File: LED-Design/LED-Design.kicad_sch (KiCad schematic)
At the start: 160 parts, among them Q1 NMOS, Q2 NMOS, Q3 NMOS, Q4 NMOS, Q5 NMOS, Q6 NMOS, Q7 NMOS, U1 74LS573, U2 74LS573, U3 74LS573, U4 74LS573, U6 74HC164

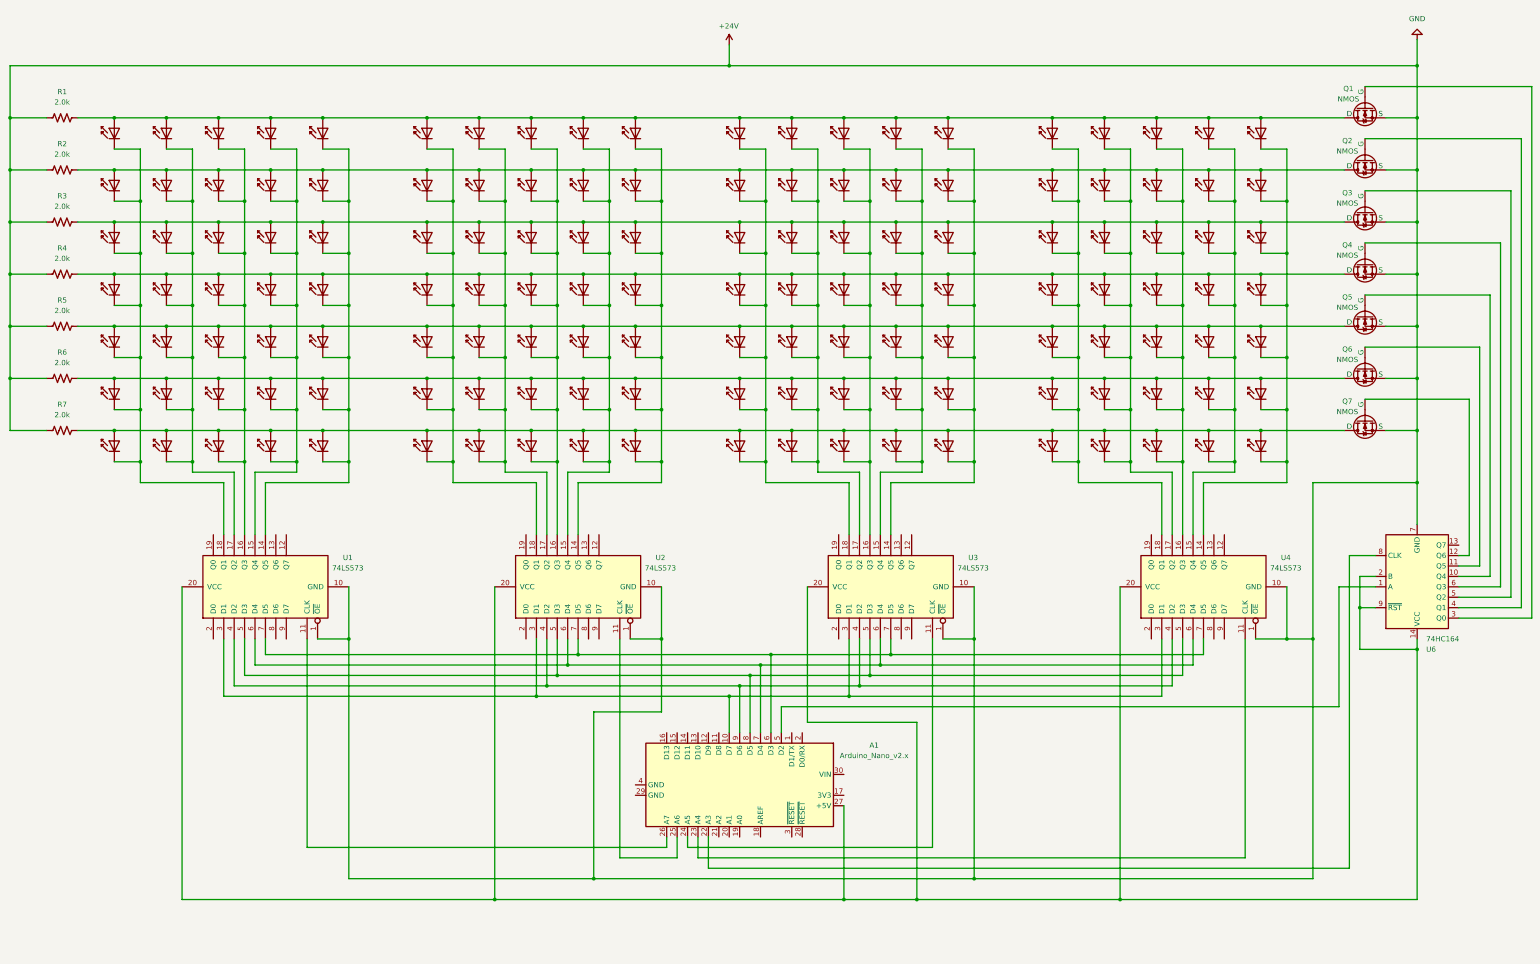
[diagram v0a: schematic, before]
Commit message: Added a Voltage divider
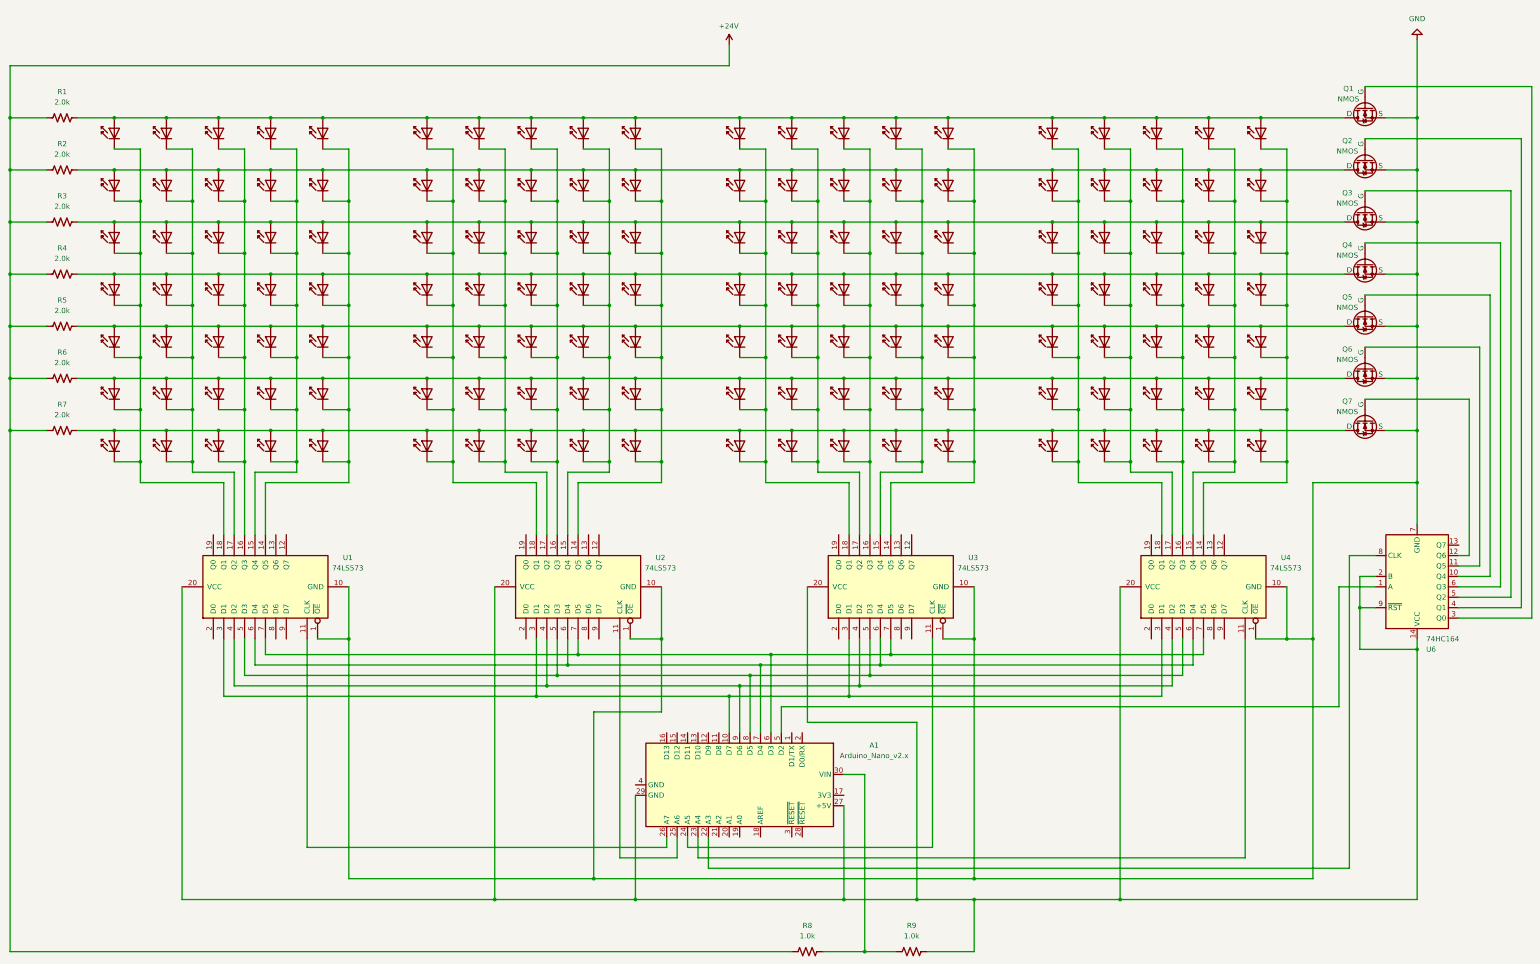
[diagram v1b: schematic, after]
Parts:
- added R8, R9: 1.0k, OptoDevice:R_LDR_5.2x5.2mm_P3.5mm_Horizontal, symbol Device:R_US
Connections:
- net +24V: now also R8.1; no longer Q1.3 (S), Q2.3 (S), Q3.3 (S), Q4.3 (S), Q5.3 (S), Q6.3 (S), Q7.3 (S), U1.1 (~{OE}), U1.10 (GND), U2.1 (~{OE}), U2.10 (GND), U3.1 (~{OE}), U3.10 (GND), U4.1 (~{OE}), U4.10 (GND), U6.7 (GND)
- net at A1.27 (+5V), U1.20 (VCC), U2.20 (VCC)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: now also A1.29 (GND), R9.2
- net at A1.30 (VIN): now also R8.2, R9.1
- new net GND: Q1.3 (S), Q2.3 (S), Q3.3 (S), Q4.3 (S), Q5.3 (S), Q6.3 (S), Q7.3 (S), U1.1 (~{OE}), U1.10 (GND), U2.1 (~{OE}), U2.10 (GND), U3.1 (~{OE}), U3.10 (GND), U4.1 (~{OE}), U4.10 (GND), U6.7 (GND)
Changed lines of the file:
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@@
 	)
 	(junction
+		(at 25.4 127)
+		(diameter 0)
+		(color 0 0 0 0)
+	)
+	(junction
 		(at 208.28 184.15)
 		(diameter 0)
@@
 	)
 	(junction
-		(at 200.66 38.1)
-		(diameter 0)
-		(color 0 0 0 0)
-	)
-	(junction
 		(at 127 88.9)
 		(diameter 0)
@@
 	)
 	(junction
+		(at 260.35 241.3)
+		(diameter 0)
+		(color 0 0 0 0)
+	)
+	(junction
 		(at 88.9 76.2)
 		(diameter 0)
@@
 	)
 	(junction
-		(at 368.3 38.1)
-		(diameter 0)
-		(color 0 0 0 0)
-	)
-	(junction
 		(at 285.75 134.62)
 		(diameter 0)
@@
 	)
 	(junction
+		(at 177.8 241.3)
+		(diameter 0)
+		(color 0 0 0 0)
+	)
+	(junction
 		(at 292.1 50.8)
 		(diameter 0)
@@
 	)
 	(junction
+		(at 233.68 254)
+		(diameter 0)
+		(color 0 0 0 0)
+	)
+	(junction
 		(at 76.2 50.8)
 		(diameter 0)
@@
 	(wire
 		(pts
+			(xy 215.9 254) (xy 25.4 254)
+		)
+		(stroke
+			(width 0)
+			(type default)
+		)
+	)
+	(wire
+		(pts
 			(xy 317.5 127) (xy 330.2 127)
 		)
@@
 	(wire
 		(pts
+			(xy 228.6 210.82) (xy 233.68 210.82)
+		)
+		(stroke
+			(width 0)
+			(type default)
+		)
+	)
+	(wire
+		(pts
 			(xy 279.4 63.5) (xy 292.1 63.5)
 		)
@@
 	(wire
 		(pts
-			(xy 246.38 241.3) (xy 295.91 241.3)
+			(xy 246.38 241.3) (xy 260.35 241.3)
 		)
 		(stroke
@@
 	(wire
 		(pts
-			(xy 368.3 31.75) (xy 368.3 38.1)
+			(xy 368.3 31.75) (xy 368.3 50.8)
 		)
 		(stroke
@@
 	(wire
 		(pts
+			(xy 177.8 215.9) (xy 177.8 241.3)
+		)
+		(stroke
+			(width 0)
+			(type default)
+		)
+	)
+	(wire
+		(pts
 			(xy 396.24 43.18) (xy 396.24 172.72)
 		)
@@
 	(wire
 		(pts
-			(xy 143.51 241.3) (xy 228.6 241.3)
+			(xy 143.51 241.3) (xy 177.8 241.3)
 		)
 		(stroke
@@
 	(wire
 		(pts
+			(xy 25.4 254) (xy 25.4 127)
+		)
+		(stroke
+			(width 0)
+			(type default)
+		)
+	)
+	(wire
+		(pts
 			(xy 76.2 50.8) (xy 88.9 50.8)
 		)
@@
 	(wire
 		(pts
+			(xy 260.35 254) (xy 260.35 241.3)
+		)
+		(stroke
+			(width 0)
+			(type default)
+		)
+	)
+	(wire
+		(pts
 			(xy 133.35 134.62) (xy 133.35 139.7)
 		)
@@
 	(wire
 		(pts
+			(xy 233.68 254) (xy 241.3 254)
+		)
+		(stroke
+			(width 0)
+			(type default)
+		)
+	)
+	(wire
+		(pts
 			(xy 63.5 63.5) (xy 76.2 63.5)
 		)
@@
 	(wire
 		(pts
+			(xy 248.92 254) (xy 260.35 254)
+		)
+		(stroke
+			(width 0)
+			(type default)
+		)
+	)
+	(wire
+		(pts
 			(xy 50.8 114.3) (xy 63.5 114.3)
 		)
@@
 	(wire
 		(pts
+			(xy 223.52 254) (xy 233.68 254)
+		)
+		(stroke
+			(width 0)
+			(type default)
+		)
+	)
+	(wire
+		(pts
 			(xy 101.6 96.52) (xy 107.95 96.52)
 		)
@@
 	(wire
 		(pts
+			(xy 260.35 241.3) (xy 295.91 241.3)
+		)
+		(stroke
+			(width 0)
+			(type default)
+		)
+	)
+	(wire
+		(pts
+			(xy 233.68 210.82) (xy 233.68 254)
+		)
+		(stroke
+			(width 0)
+			(type default)
+		)
+	)
+	(wire
+		(pts
 			(xy 76.2 121.92) (xy 82.55 121.92)
 		)
@@
 	(wire
 		(pts
-			(xy 200.66 38.1) (xy 368.3 38.1)
-		)
-		(stroke
-			(width 0)
-			(type default)
-		)
-	)
-	(wire
-		(pts
 			(xy 240.03 152.4) (xy 240.03 139.7)
 		)
@@
 	(wire
 		(pts
-			(xy 368.3 50.8) (xy 368.3 38.1)
-		)
-		(stroke
-			(width 0)
-			(type default)
-		)
-	)
-	(wire
-		(pts
 			(xy 139.7 127) (xy 152.4 127)
 		)
@@
 	(wire
 		(pts
+			(xy 177.8 241.3) (xy 228.6 241.3)
+		)
+		(stroke
+			(width 0)
+			(type default)
+		)
+	)
+	(wire
+		(pts
 			(xy 41.91 127) (xy 50.8 127)
 		)
@@
 	)
 	(symbol
+		(lib_id "Device:R_US")
+		(at 245.11 254 90)
+		(unit 1)
+		(exclude_from_sim no)
+		(in_bom yes)
+		(on_board yes)
+		(dnp no)
+		(fields_autoplaced yes)
+		(property "Reference" "R9"
+			(at 245.11 247.65 90)
+			(effects
+				(font
+					(size 1.27 1.27)
+				)
+			)
+		)
+		(property "Value" "1.0k"
+			(at 245.11 250.19 90)
+			(effects
+				(font
+					(size 1.27 1.27)
+				)
+			)
+		)
+		(property "Footprint" "OptoDevice:R_LDR_5.2x5.2mm_P3.5mm_Horizontal"
+			(at 245.364 252.984 90)
+			(effects
+				(font
+					(size 1.27 1.27)
+				)
+				(hide yes)
+			)
+		)
+		(property "Datasheet" "~"
+			(at 245.11 254 0)
+			(effects
+				(font
+					(size 1.27 1.27)
+				)
+				(hide yes)
+			)
+		)
+		(property "Description" "Resistor, US symbol"
+			(at 245.11 254 0)
+			(effects
+				(font
+					(size 1.27 1.27)
+				)
+				(hide yes)
+			)
+		)
+		(pin "1"
+		)
+		(pin "2"
+		)
+		(instances
+			(project "LED-Design"
+				(path "/f4f73743-e943-40e7-b3a9-52df178c6ab8"
+					(reference "R9")
+					(unit 1)
+				)
+			)
+		)
+	)
+	(symbol
 		(lib_id "LED:IR204A")
 		(at 76.2 78.74 90)
@@
 					(unit 1)
 				)
+			)
+		)
+	)
+	(symbol
+		(lib_id "Device:R_US")
+		(at 219.71 254 90)
+		(unit 1)
+		(exclude_from_sim no)
+		(in_bom yes)
+		(on_board yes)
+		(dnp no)
+		(fields_autoplaced yes)
+		(property "Reference" "R8"
+			(at 219.71 247.65 90)
+			(effects
+				(font
+					(size 1.27 1.27)
+				)
+			)
+		)
+		(property "Value" "1.0k"
+			(at 219.71 250.19 90)
+			(effects
+				(font
+					(size 1.27 1.27)
+				)
+			)
+		)
+		(property "Footprint" "OptoDevice:R_LDR_5.2x5.2mm_P3.5mm_Horizontal"
+			(at 219.964 252.984 90)
+			(effects
+				(font
+					(size 1.27 1.27)
+				)
+				(hide yes)
+			)
+		)
+		(property "Datasheet" "~"
+			(at 219.71 254 0)
+			(effects
+				(font
+					(size 1.27 1.27)
+				)
+				(hide yes)
+			)
+		)
+		(property "Description" "Resistor, US symbol"
+			(at 219.71 254 0)
+			(effects
+				(font
+					(size 1.27 1.27)
+				)
+				(hide yes)
+			)
+		)
+		(pin "1"
+		)
+		(pin "2"
+		)
+		(instances
+			(project "LED-Design"
+				(path "/f4f73743-e943-40e7-b3a9-52df178c6ab8"
+					(reference "R8")
+					(unit 1)
+				)

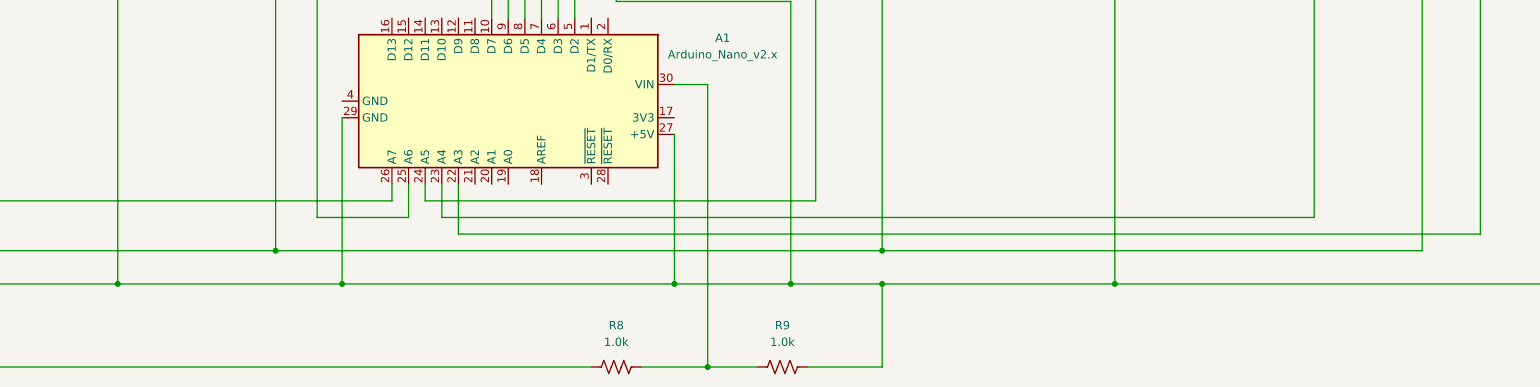
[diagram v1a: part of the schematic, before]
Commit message: Added all components to the schematic and linked them to their footprints
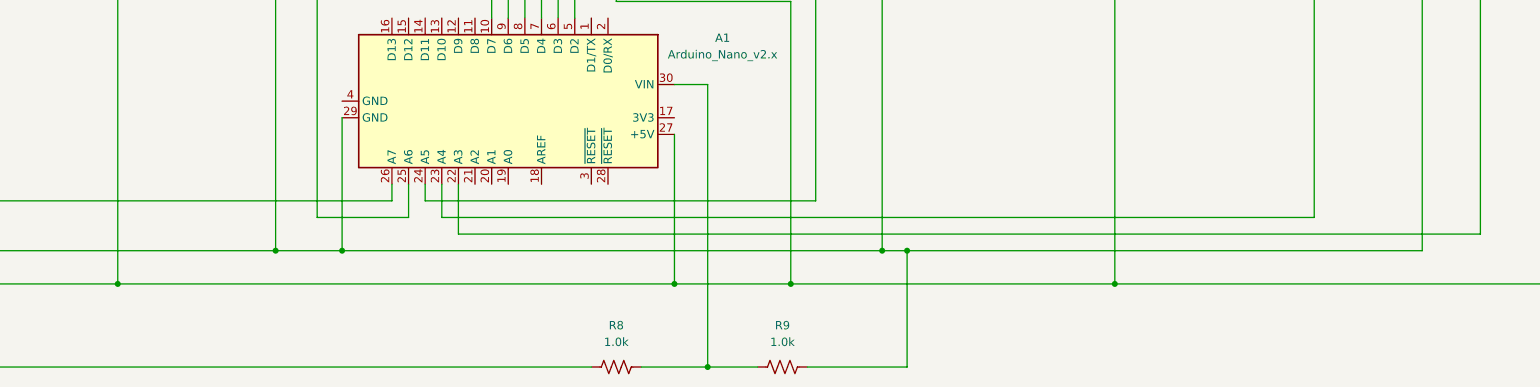
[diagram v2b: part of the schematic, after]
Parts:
- Q1, Q2, Q3, Q4, Q5, Q6, Q7: footprint (none) -> Package_TO_SOT_THT:TO-220-3_Vertical
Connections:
- net GND: now also A1.29 (GND), R9.2
- net at A1.27 (+5V), U1.20 (VCC), U2.20 (VCC)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: no longer A1.29 (GND), R9.2
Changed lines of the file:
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@@
 	)
 	(junction
+		(at 264.16 236.22)
+		(diameter 0)
+		(color 0 0 0 0)
+	)
+	(junction
 		(at 215.9 63.5)
 		(diameter 0)
@@
 	)
 	(junction
+		(at 177.8 236.22)
+		(diameter 0)
+		(color 0 0 0 0)
+	)
+	(junction
 		(at 246.38 241.3)
 		(diameter 0)
@@
 	)
 	(junction
-		(at 260.35 241.3)
-		(diameter 0)
-		(color 0 0 0 0)
-	)
-	(junction
 		(at 88.9 76.2)
 		(diameter 0)
@@
 	)
 	(junction
-		(at 177.8 241.3)
-		(diameter 0)
-		(color 0 0 0 0)
-	)
-	(junction
 		(at 292.1 50.8)
 		(diameter 0)
@@
 	(wire
 		(pts
-			(xy 246.38 241.3) (xy 260.35 241.3)
-		)
-		(stroke
-			(width 0)
-			(type default)
-		)
-	)
-	(wire
-		(pts
 			(xy 69.85 58.42) (xy 69.85 71.12)
 		)
@@
 	(wire
 		(pts
+			(xy 177.8 215.9) (xy 177.8 236.22)
+		)
+		(stroke
+			(width 0)
+			(type default)
+		)
+	)
+	(wire
+		(pts
 			(xy 260.35 83.82) (xy 260.35 96.52)
 		)
@@
 	(wire
 		(pts
-			(xy 177.8 215.9) (xy 177.8 241.3)
-		)
-		(stroke
-			(width 0)
-			(type default)
-		)
-	)
-	(wire
-		(pts
 			(xy 396.24 43.18) (xy 396.24 172.72)
 		)
@@
 	(wire
 		(pts
-			(xy 143.51 241.3) (xy 177.8 241.3)
-		)
-		(stroke
-			(width 0)
-			(type default)
-		)
-	)
-	(wire
-		(pts
 			(xy 107.95 109.22) (xy 107.95 121.92)
 		)
@@
 	(wire
 		(pts
-			(xy 260.35 236.22) (xy 342.9 236.22)
+			(xy 260.35 236.22) (xy 264.16 236.22)
 		)
 		(stroke
@@
 	(wire
 		(pts
-			(xy 260.35 254) (xy 260.35 241.3)
-		)
-		(stroke
-			(width 0)
-			(type default)
-		)
-	)
-	(wire
-		(pts
 			(xy 133.35 134.62) (xy 133.35 139.7)
 		)
@@
 	(wire
 		(pts
-			(xy 167.64 236.22) (xy 260.35 236.22)
+			(xy 167.64 236.22) (xy 177.8 236.22)
+		)
+		(stroke
+			(width 0)
+			(type default)
+		)
+	)
+	(wire
+		(pts
+			(xy 177.8 236.22) (xy 260.35 236.22)
 		)
 		(stroke
@@
 	(wire
 		(pts
-			(xy 248.92 254) (xy 260.35 254)
+			(xy 248.92 254) (xy 264.16 254)
 		)
 		(stroke
@@
 	(wire
 		(pts
+			(xy 264.16 254) (xy 264.16 236.22)
+		)
+		(stroke
+			(width 0)
+			(type default)
+		)
+	)
+	(wire
+		(pts
 			(xy 326.39 231.14) (xy 193.04 231.14)
 		)
@@
 	(wire
 		(pts
+			(xy 264.16 236.22) (xy 342.9 236.22)
+		)
+		(stroke
+			(width 0)
+			(type default)
+		)
+	)
+	(wire
+		(pts
 			(xy 222.25 109.22) (xy 222.25 121.92)
 		)
@@
 	(wire
 		(pts
-			(xy 260.35 241.3) (xy 295.91 241.3)
+			(xy 246.38 241.3) (xy 295.91 241.3)
 		)
 		(stroke
@@
 	(wire
 		(pts
-			(xy 177.8 241.3) (xy 228.6 241.3)
+			(xy 143.51 241.3) (xy 228.6 241.3)
 		)
 		(stroke
@@
 			)
 		)
-		(property "Footprint" ""
+		(property "Footprint" "Package_TO_SOT_THT:TO-220-3_Vertical"
 			(at 353.06 78.74 0)
 			(effects
@@
 			)
 		)
-		(property "Footprint" ""
+		(property "Footprint" "Package_TO_SOT_THT:TO-220-3_Vertical"
 			(at 353.06 91.44 0)
 			(effects
@@
 			)
 		)
-		(property "Footprint" ""
+		(property "Footprint" "Package_TO_SOT_THT:TO-220-3_Vertical"
 			(at 353.06 116.84 0)
 			(effects
@@
 			)
 		)
-		(property "Footprint" ""
+		(property "Footprint" "Package_TO_SOT_THT:TO-220-3_Vertical"
 			(at 353.06 129.54 0)
 			(effects
@@
 			)
 		)
-		(property "Footprint" ""
+		(property "Footprint" "Package_TO_SOT_THT:TO-220-3_Vertical"
 			(at 353.06 66.04 0)
 			(effects
@@
 			)
 		)
-		(property "Footprint" ""
+		(property "Footprint" "Package_TO_SOT_THT:TO-220-3_Vertical"
 			(at 353.06 53.34 0)
 			(effects
@@
 			)
 		)
-		(property "Footprint" ""
+		(property "Footprint" "Package_TO_SOT_THT:TO-220-3_Vertical"
 			(at 353.06 104.14 0)
 			(effects

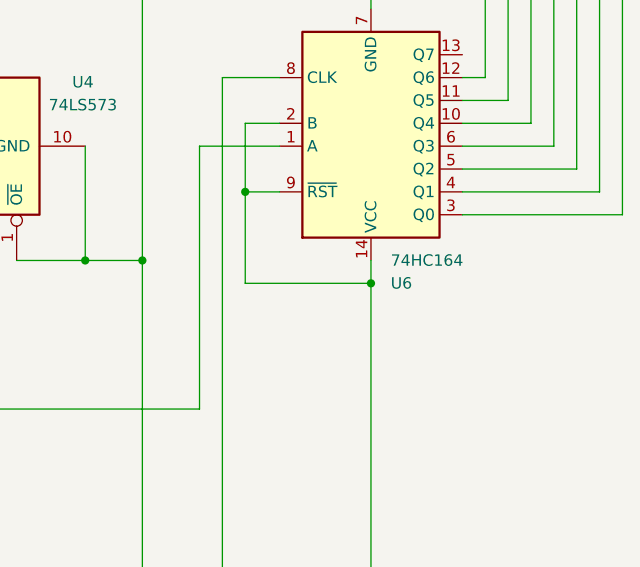
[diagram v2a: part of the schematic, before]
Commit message: Used the distribute function in PCB Design to correctly align all the LEDs in their matrix. Used an 8mm gap between all LEDs
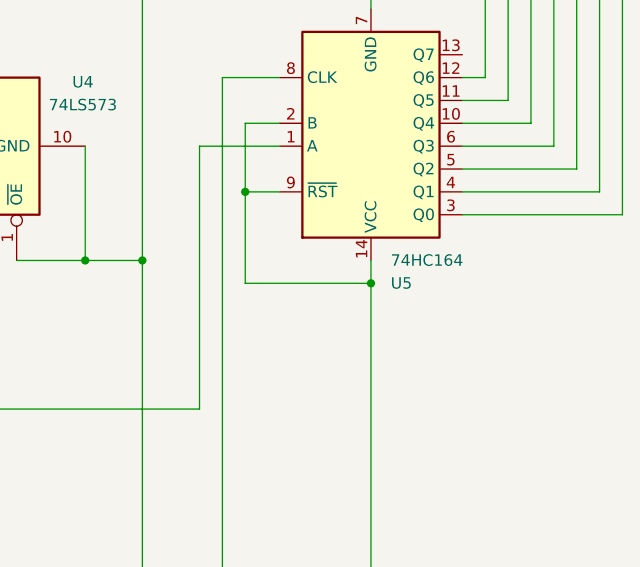
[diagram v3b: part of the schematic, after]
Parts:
- renumbered U6 to U5
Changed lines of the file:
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@@
 		(on_board yes)
 		(dnp no)
-		(property "Reference" "U6"
+		(property "Reference" "U5"
 			(at 370.4941 180.34 0)
 			(effects
@@
 			(project "LED-Design"
 				(path "/f4f73743-e943-40e7-b3a9-52df178c6ab8"
-					(reference "U6")
+					(reference "U5")
 					(unit 1)
 				)
